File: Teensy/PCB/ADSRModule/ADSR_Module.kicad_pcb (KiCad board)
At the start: 2 copper layers, 53.3 x 106.7 mm, 41 parts, among them J1 Power_Connector_2x3, SW1 Mode_Switch, U1 Teensy4.0

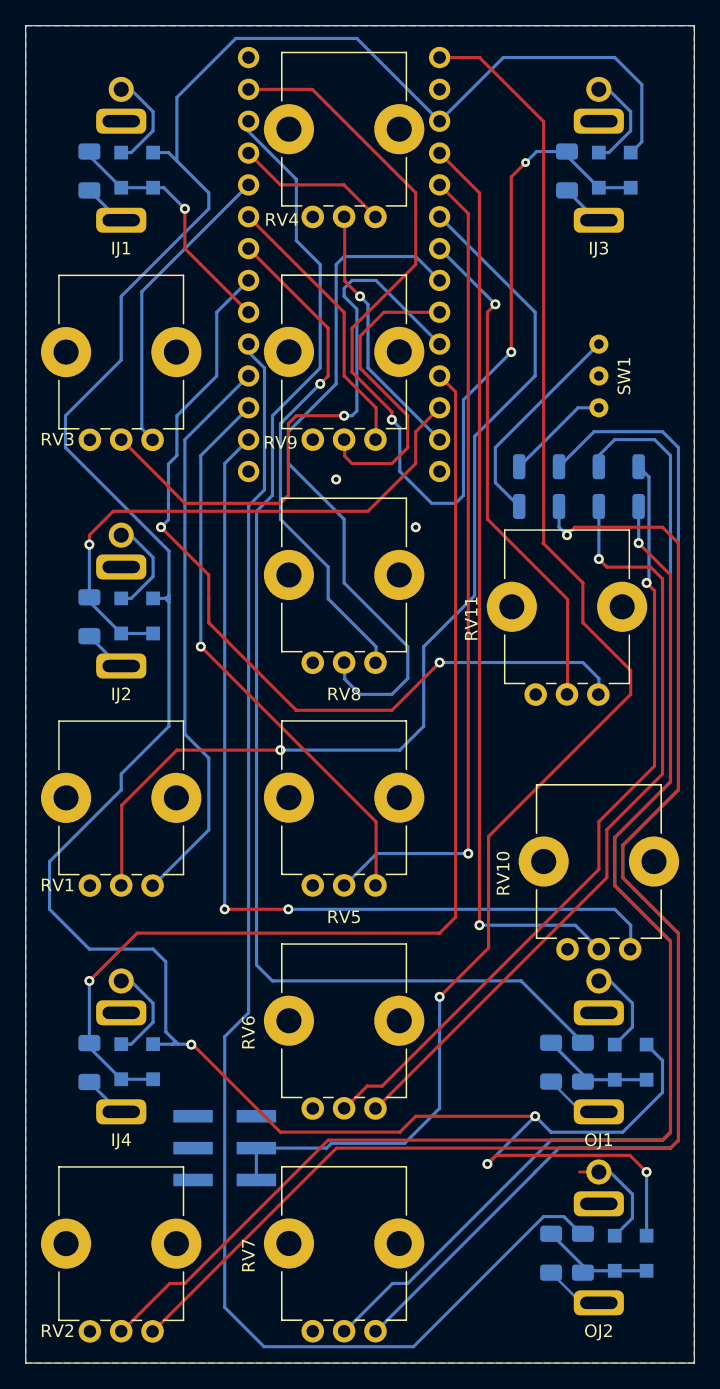
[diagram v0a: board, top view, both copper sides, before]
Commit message: Made NPTH holes 0.5mm bigger; adjusted diode pads for better solderability
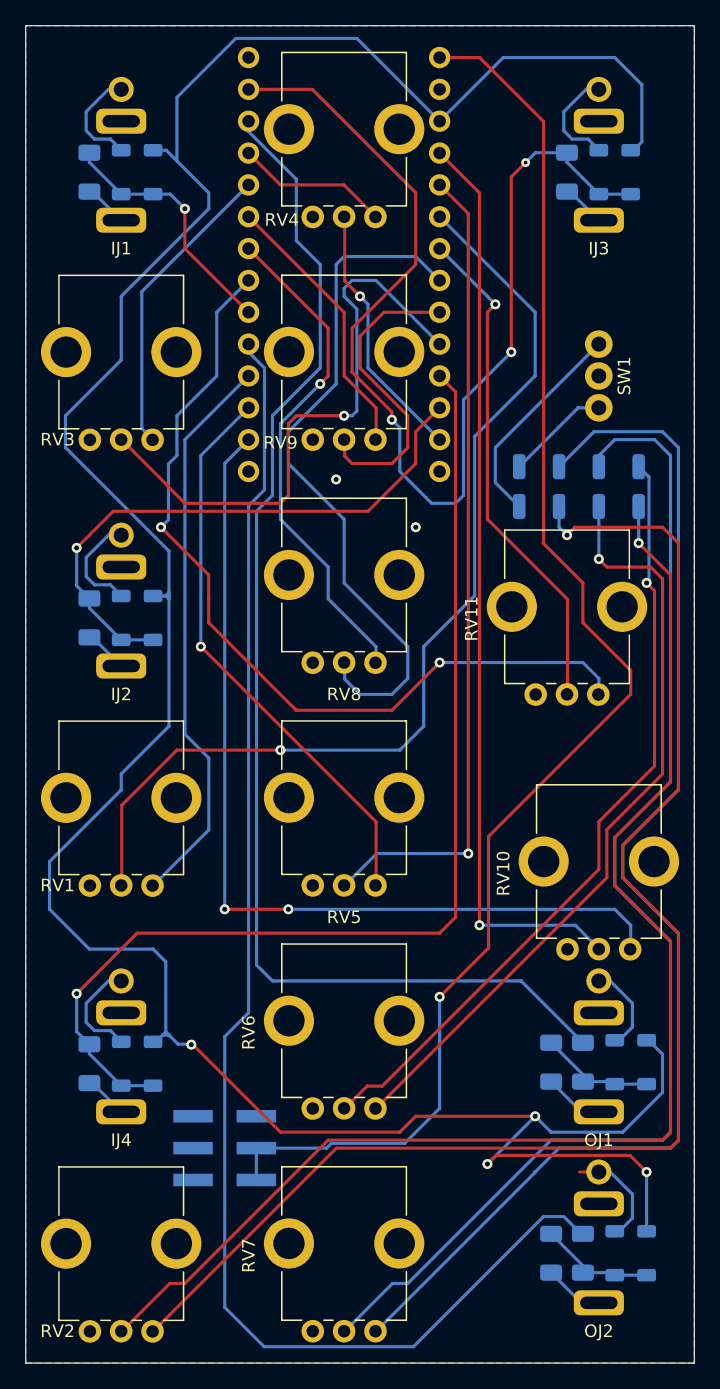
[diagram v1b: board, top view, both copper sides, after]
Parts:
- ID1, ID2, ID3, ID4, ID5, ID6, ID7, ID8, OD1, OD2, OD3, OD4: footprint Diode_SMD:D_SOD-123F -> Misc:D_SOD-123 Handsolder
- moved ID1 0.16 mm to (78.7, 47.2)
- moved ID2 0.16 mm to (81.3, 47.2)
- moved ID3 0.16 mm to (78.7, 82.8)
- moved ID4 0.16 mm to (81.3, 82.8)
- moved ID5 0.16 mm to (116.8, 47.2)
- moved ID6 0.16 mm to (119.4, 47.2)
- moved ID7 0.16 mm to (78.7, 118.4)
- moved ID8 0.16 mm to (81.3, 118.4)
- moved IR4 0.10 mm to (76.2, 118.4)
- moved IR1 0.10 mm to (76.2, 47.2)
- moved IR3 0.10 mm to (114.3, 47.2)
- moved IR2 0.10 mm to (76.2, 82.8)
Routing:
- net GND: track 48.4 -> 49.8 mm
- net /T16: track 86.5 -> 87.8 mm
- net /T15: track 45.1 -> 46.4 mm
